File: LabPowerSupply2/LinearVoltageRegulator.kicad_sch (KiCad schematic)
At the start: 17 parts, among them Q1_LVR1 PJA3404_R1_00001, Q2_LVR1 PJA3404_R1_00001, Q3_LVR1 PJA3404_R1_00001

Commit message: Updated Version 2
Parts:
- removed C_INV1: 100n, Capacitor_SMD:C_0603_1608Metric, symbol Device:C
- removed Inverter1: 74AHC04, Package_SO:SSOP-14_5.3x6.2mm_P0.65mm, symbol 74xx:74AHC04
- added Q4_LVR1: PJA3404_R1_00001, SamacSys_Parts:SOT95P240X110-3N, symbol SamacSys_Parts:PJA3404_R1_00001
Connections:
- net 3.3 Volts: now also R13_LVR1.1
- net GND: now also Q4_LVR1.2 (S); no longer R13_LVR1.1
- net On/Off: now also R2_LVR1.2
- net at R2_LVR1.1: now also Q4_LVR1.1 (G); no longer Q1_LVR1.1 (G)
- new net: Q1_LVR1.1 (G), Q4_LVR1.3 (D)
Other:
- moved on the sheet: C1_LVR1, C3_LVR1, C4_LVR1, D_LVR1, Linear1, Linear1_1, Q1_LVR1, Q2_LVR1, Q3_LVR1, R11_LVR1, R12_LVR1, R13_LVR1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

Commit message: Beautifing the Schematic
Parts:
- removed Linear1: LT3083ET#PBF, SamacSys_Parts:TO170P457X1022X2306-5P, symbol SamacSys_Parts:LT3083ET#PBF
- added R5_LVR1: 10k, symbol Device:R_US
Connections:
- net 3.3 Volts: now also R5_LVR1.1
- net Charge: now also C4_LVR1.1
- net at D_LVR1.1 (K), Linear1_1.4 (SET), R12_LVR1.1: no longer C4_LVR1.1
- net at Q1_LVR1.1 (G), Q4_LVR1.3 (D): now also R5_LVR1.2
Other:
- note added: "Prevents Latch-up"
- note added: "Replaces Inverter"
- moved on the sheet: C1_LVR1, C3_LVR1, C4_LVR1, D_LVR1, Linear1_1, Q1_LVR1, Q2_LVR1, Q3_LVR1, Q4_LVR1, R11_LVR1, R12_LVR1, R2_LVR1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

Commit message: Fixed the Beautified Schematics
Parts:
- R5_LVR1: footprint (none) -> Resistor_SMD:R_0603_1608Metric
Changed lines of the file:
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@@
       (effects (font (size 1.27 1.27)) (justify left))
     )
-    (property "Footprint" "" (id 2) (at 134.366 65.024 90)
+    (property "Footprint" "Resistor_SMD:R_0603_1608Metric" (id 2) (at 134.366 65.024 90)
       (effects (font (size 1.27 1.27)) hide)
     )

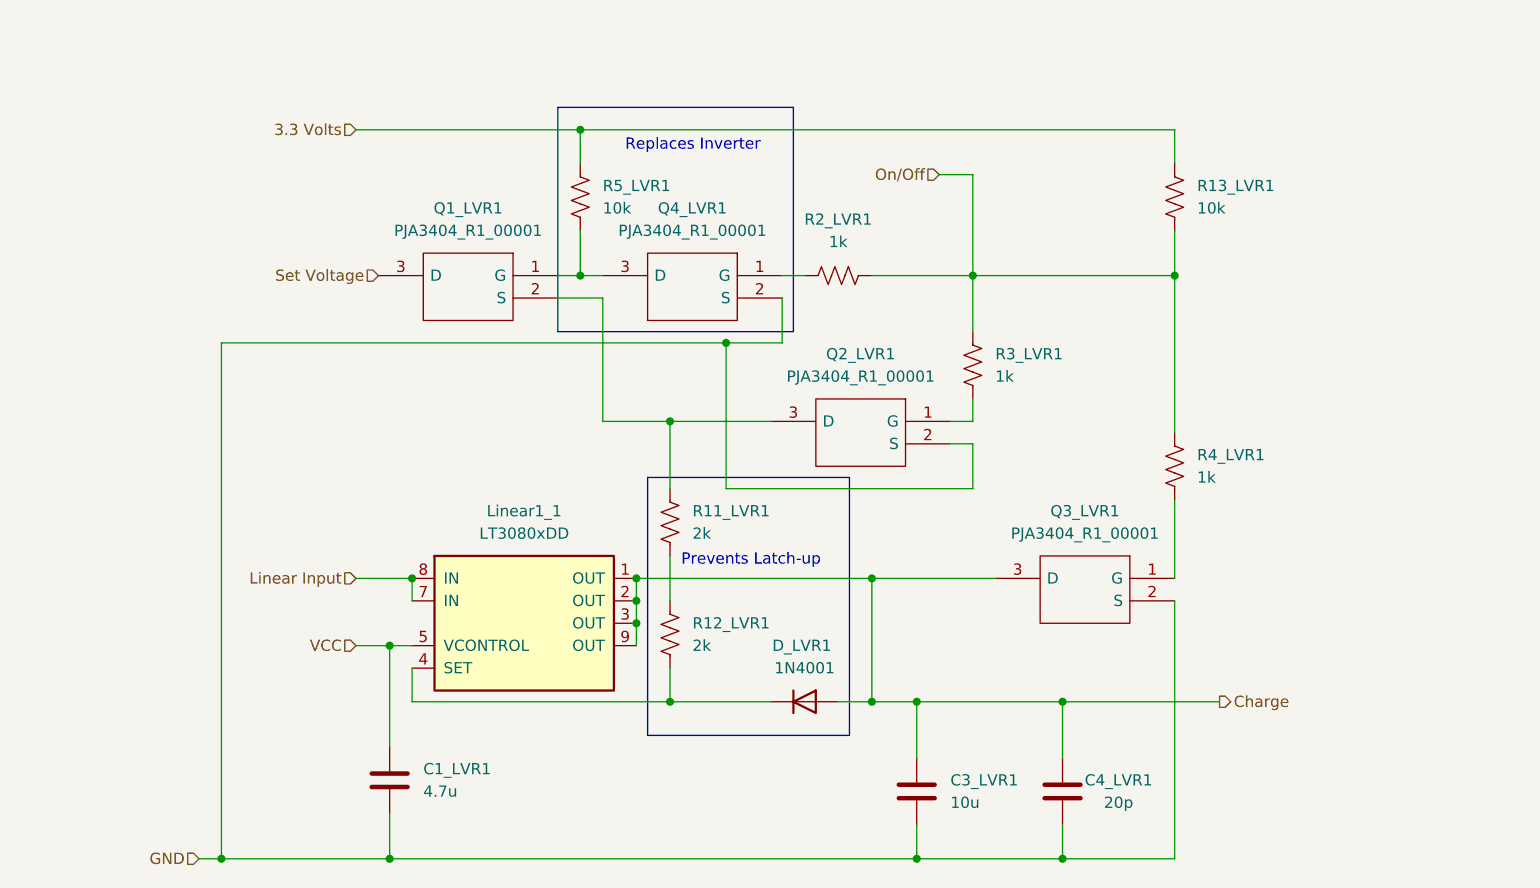
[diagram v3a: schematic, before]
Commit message: Changed symbols to actual MOSFETs
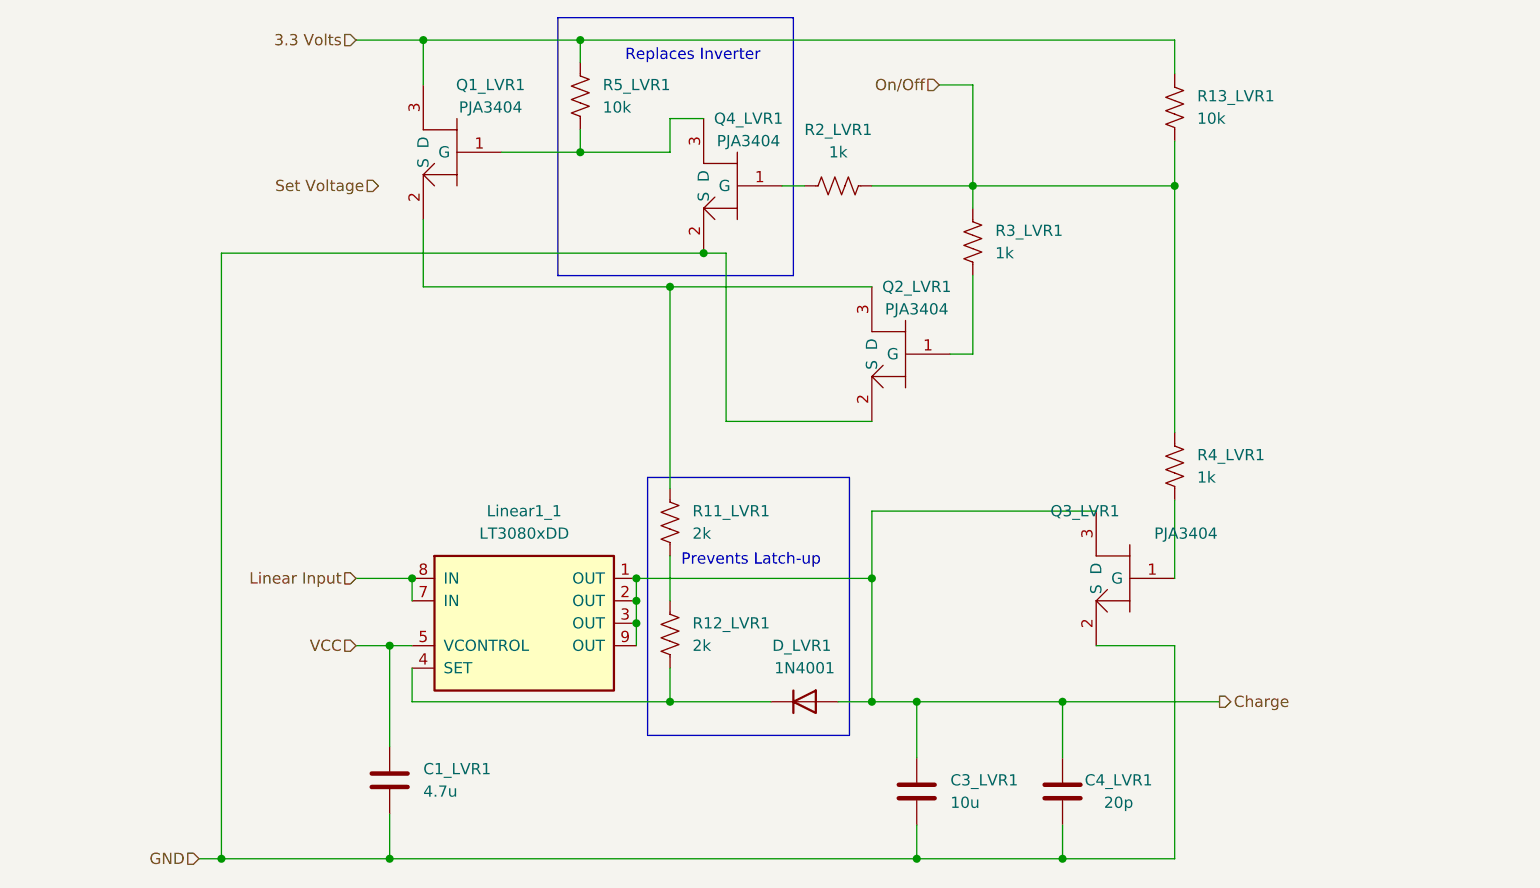
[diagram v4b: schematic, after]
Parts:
- Q1_LVR1: value PJA3404_R1_00001 -> PJA3404
- Q2_LVR1, Q3_LVR1, Q4_LVR1: value PJA3404_R1_00001 -> PJA3404; symbol SamacSys_Parts:PJA3404_R1_00001 -> SamacSys_Parts:PJA3404
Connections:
- net 3.3 Volts: now also Q1_LVR1.3 (D)
- net Set Voltage: no longer Q1_LVR1.3 (D)
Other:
- moved on the sheet: R13_LVR1, R2_LVR1, R3_LVR1, R5_LVR1
